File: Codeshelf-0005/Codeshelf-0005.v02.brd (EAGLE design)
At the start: 140.1 x 99 mm, 53 parts, among them J1 M05X2PTH, J2 RJ45-8PTH, J3-WAKE M02PTH, J4 RJ45-8PTH, J5 HEADER-2X-2.54MM, U1 ZSFM201-1A, U2 MAX232SOIC16, U3 RS485SOIC, U4 ULN2003AD, U5 MIC94061C6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

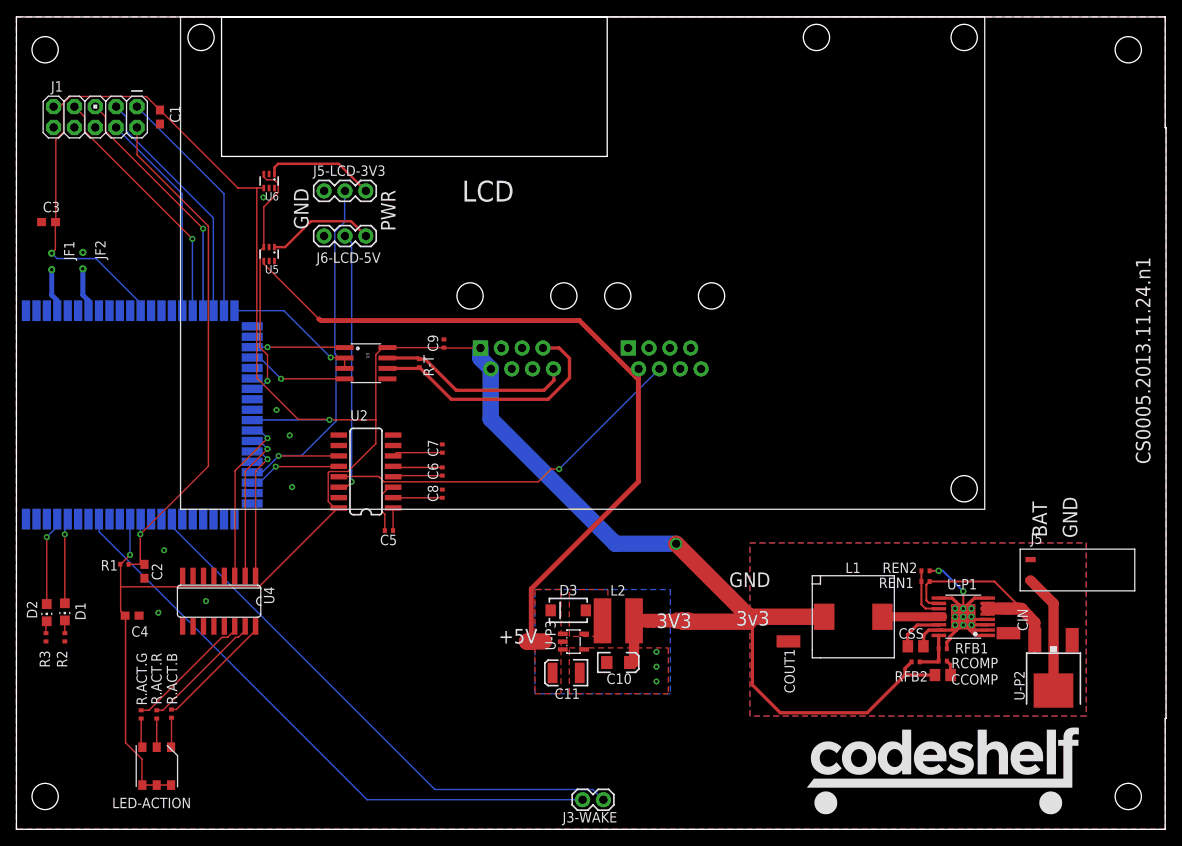
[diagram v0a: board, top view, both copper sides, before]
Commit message: Remove 5V SMPS
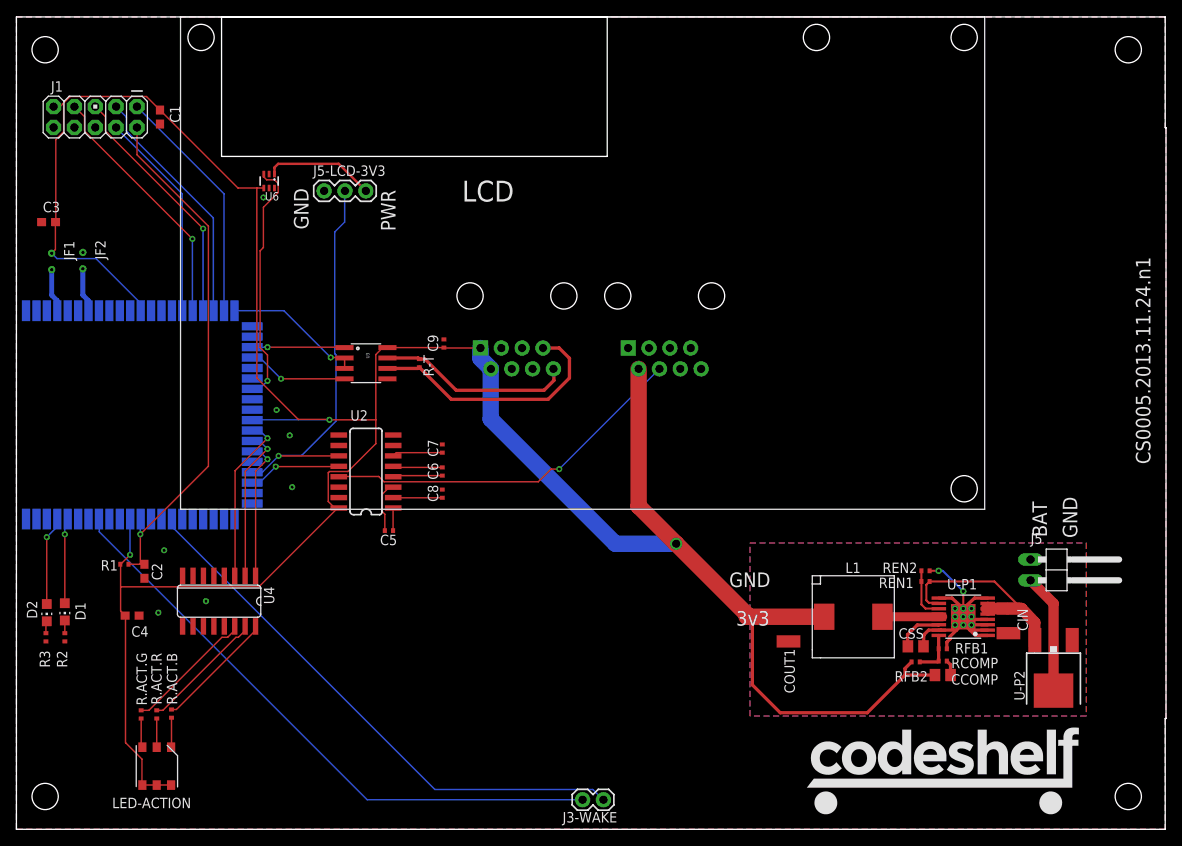
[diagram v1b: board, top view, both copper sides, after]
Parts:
- removed C10: 10uF, SparkFun:EIA3216
- removed C11: 68uF, SparkFun:EIA3528
- removed D3: MBRA140, SparkFun:SMA-DIODE
- removed J6-LCD-5V: (no value), SparkFun-Connectors:1X03
- removed L2: 47uH, SparkFun:CR54
- removed U-P3: NCP1402, SparkFun:SOT23-5
- removed U5: MIC94061C6, GW-devices:SC70-6L
- J5: value HEADER-2X-2.54MM -> (none); device GW-devices:HEADER-2X-RA-2.54MM -> pinhead:1X02/90
- moved J5 3.81 mm to (137.4, 36.6), turned to 270 degrees
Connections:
- removed net +5V: C11.A, D3.C, J2.2, U-P3.1, U-P3.2, U5.4
- removed net N$13: J6-LCD-5V.3, U5.1
- removed net N$5: D3.A, L2.P$2, U-P3.5
- removed net T1OUT: J6-LCD-5V.2, U2.14
- net +3V3: now also J2.2; no longer C10.A, L2.P$1
- net GND: no longer C10.C, C11.C, J6-LCD-5V.1, U-P3.4, U5.2, U5.5
- net N$9: no longer U5.3
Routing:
- net +5V: track 93.0 -> 0.00 mm
- net T1OUT: track 32.1 -> 0.00 mm, vias 1 -> 0
- net N$13: track 13.2 -> 0.00 mm
- net +3V3: track 349.7 -> 348.3 mm
- net GND: vias 21 -> 18
- removed copper zone on layer 1, net +5V
- removed copper zone on layer 1, net N$5
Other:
- board text removed: "+5V"
- board text removed: "3V3"
